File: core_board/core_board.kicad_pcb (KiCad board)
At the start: 2 copper layers, 85.5 x 104 mm, 111 parts, among them J1 Molex_Megafit_02, J10 Conn_01x04_Pin, J11 Conn_01x02_Pin, J12 Conn_01x02_Pin, J13 Conn_01x03_Pin, J14 Conn_01x02_Pin, J15 Conn_01x02_Pin, J16 Conn_01x03_Pin, J2 RJ45_LED_Shielded, J3 Conn_01x02_Pin, J4Serv1 Conn_01x04_Pin, J5 Conn_01x04_Pin, J6 Conn_01x02_Pin, J8 Conn_01x04_Pin, J9 Conn_01x02_Pin, Q1 TPC8132_LQS, Q18 BSS138, Q19 BSS138, Q2 BSS138, Q20 BSS138, Q21 BSS138, Q3 BSS138, Q4 BSS138, Q5 BSS138, Q6 BSS138, Q7 BSS138, SW1 SW_Push, SW2 SW_Push, SW3 SW_Push, SW4 SW_Push, U1 AP63301WU7, U4 BD9G401EFJ-E2

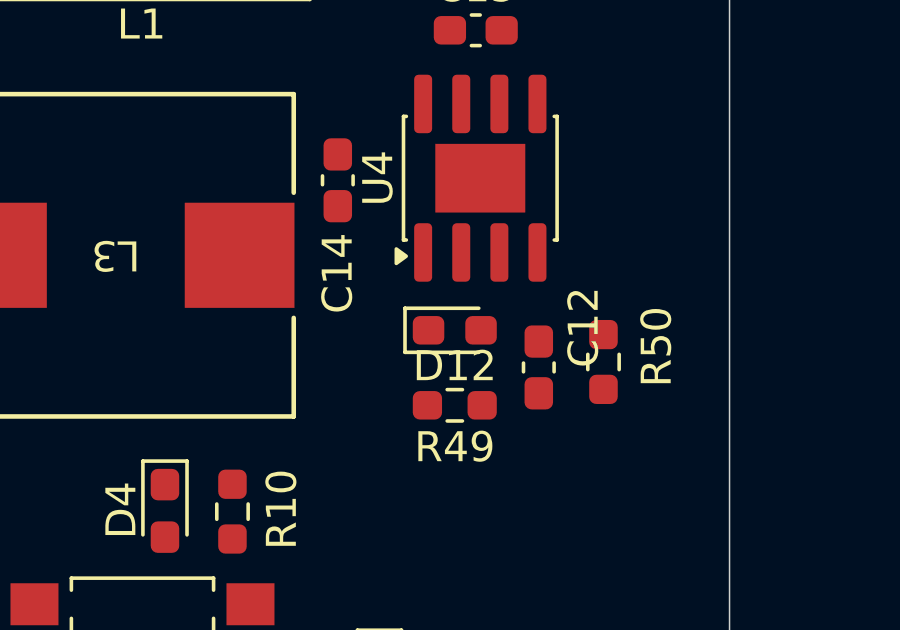
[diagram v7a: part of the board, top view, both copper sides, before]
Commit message: Fix buck circuit values
nothing had values, so I added them
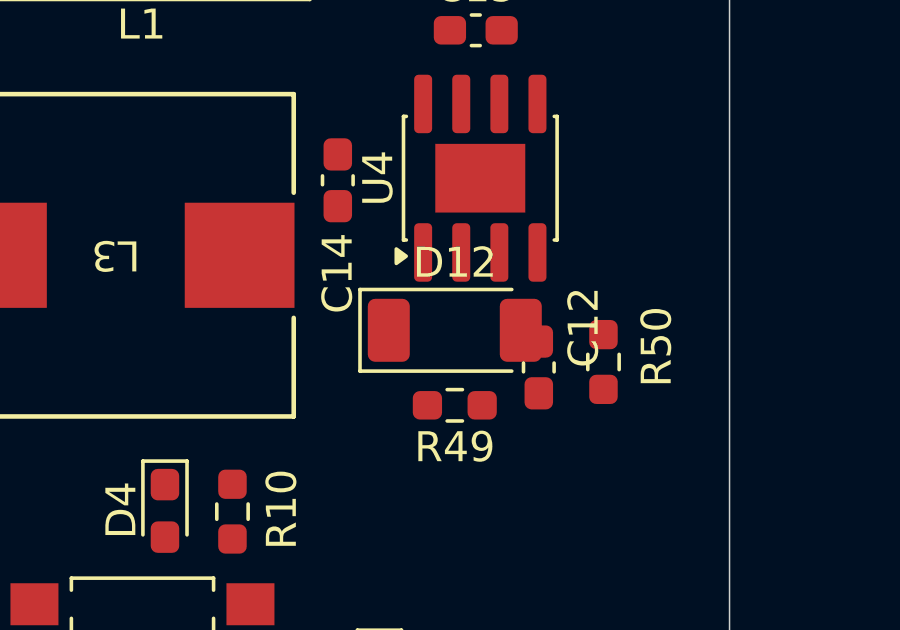
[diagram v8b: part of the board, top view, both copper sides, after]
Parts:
- C12: value C_Small -> 0.01uF
- C13: value C_Small -> 47uF
- C14: value C_Small -> 0.1uF
- C15: value C_Small -> 10uF
- D12: value MMSZ5240BT1G -> PMEG4050EP,115; footprint LED_SMD:LED_0603_1608Metric_Pad1.05x0.95mm_HandSolder -> Diode_SMD:D_SOD-128
- R48: value R_US -> 160k
- R49: value R_US -> 30k
- R50: value R_US -> 4.7k
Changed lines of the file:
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@@
 		)
 	)
-	(footprint "LED_SMD:LED_0603_1608Metric_Pad1.05x0.95mm_HandSolder"
+	(footprint "Diode_SMD:D_SOD-128"
 		(layer "F.Cu")
 		(at 183.8422 58.8626)
-		(descr "LED SMD 0603 (1608 Metric), square (rectangular) end terminal, IPC-7351 nominal, (Body size source: http://www.tortai-tech.com/upload/download/2011102023233369053.pdf)")
-		(tags "LED handsolder")
+		(descr "D_SOD-128 (CFP5 SlimSMAW), https://assets.nexperia.com/documents/outline-drawing/SOD128.pdf")
+		(tags "D_SOD-128")
 		(property "Reference" "D12"
-			(at 0 1.2 0)
+			(at 0 -2.25 0)
 			(layer "F.SilkS")
 			(effects
@@
 			)
 		)
-		(property "Value" "MMSZ5240BT1G"
-			(at -0.0125 1.5 0)
+		(property "Value" "PMEG4050EP,115"
+			(at 0 2.25 0)
 			(layer "F.Fab")
 			(effects
@@
 			)
 		)
-		(property "Datasheet" "https://www.onsemi.com/pdf/datasheet/mmsz5221bt1-d.pdf"
+		(property "Datasheet" "https://assets.nexperia.com/documents/data-sheet/PMEG4050EP.pdf"
 			(at 0 0 0)
+			(unlocked yes)
 			(layer "F.Fab")
 			(hide yes)
@@
 				(font
 					(size 1.27 1.27)
+					(thickness 0.15)
 				)
 			)
@@
 		(property "Description" ""
 			(at 0 0 0)
+			(unlocked yes)
 			(layer "F.Fab")
 			(hide yes)
@@
 				(font
 					(size 1.27 1.27)
-				)
-			)
-		)
-		(property "KiLib_Generator" "SMD_2terminal_chip_molded"
-			(at 0 0 0)
-			(layer "F.SilkS")
-			(hide yes)
-			(effects
-				(font
-					(size 1 1)
 					(thickness 0.15)
 				)
@@
 		(duplicate_pad_numbers_are_jumpers no)
 		(fp_line
-			(start -1.66 -0.735)
-			(end -1.66 0.735)
+			(start -3.16 -1.36)
+			(end -3.16 1.36)
 			(stroke
 				(width 0.12)
@@
 		)
 		(fp_line
-			(start -1.66 0.735)
-			(end 0.8 0.735)
+			(start -3.16 -1.36)
+			(end 1.9 -1.36)
 			(stroke
 				(width 0.12)
@@
 		)
 		(fp_line
-			(start 0.8 -0.735)
-			(end -1.66 -0.735)
+			(start -3.16 1.36)
+			(end 1.9 1.36)
 			(stroke
 				(width 0.12)
@@
 			(layer "F.SilkS")
 		)
-		(fp_rect
-			(start -1.65 -0.73)
-			(end 1.65 0.73)
+		(fp_line
+			(start -3.15 -1.5)
+			(end -3.15 1.5)
 			(stroke
 				(width 0.05)
 				(type solid)
 			)
-			(fill no)
 			(layer "F.CrtYd")
 		)
 		(fp_line
-			(start -0.8 -0.1)
-			(end -0.8 0.4)
+			(start -3.15 -1.5)
+			(end 3.15 -1.5)
+			(stroke
+				(width 0.05)
+				(type solid)
+			)
+			(layer "F.CrtYd")
+		)
+		(fp_line
+			(start 3.15 -1.5)
+			(end 3.15 1.5)
+			(stroke
+				(width 0.05)
+				(type solid)
+			)
+			(layer "F.CrtYd")
+		)
+		(fp_line
+			(start 3.15 1.5)
+			(end -3.15 1.5)
+			(stroke
+				(width 0.05)
+				(type solid)
+			)
+			(layer "F.CrtYd")
+		)
+		(fp_line
+			(start -1.9 -1.25)
+			(end 1.9 -1.25)
 			(stroke
 				(width 0.1)
@@
 		)
 		(fp_line
-			(start -0.8 0.4)
-			(end 0.8 0.4)
+			(start -1.9 1.25)
+			(end -1.9 -1.25)
 			(stroke
 				(width 0.1)
@@
 		)
 		(fp_line
-			(start -0.5 -0.4)
-			(end -0.8 -0.1)
+			(start -0.75 0)
+			(end -0.35 0)
 			(stroke
 				(width 0.1)
@@
 		)
 		(fp_line
-			(start 0.8 -0.4)
-			(end -0.5 -0.4)
+			(start -0.35 0)
+			(end -0.35 -0.55)
 			(stroke
 				(width 0.1)
@@
 		)
 		(fp_line
-			(start 0.8 0.4)
-			(end 0.8 -0.4)
+			(start -0.35 0)
+			(end -0.35 0.55)
+			(stroke
+				(width 0.1)
+				(type solid)
+			)
+			(layer "F.Fab")
+		)
+		(fp_line
+			(start -0.35 0)
+			(end 0.25 -0.4)
+			(stroke
+				(width 0.1)
+				(type solid)
+			)
+			(layer "F.Fab")
+		)
+		(fp_line
+			(start 0.25 -0.4)
+			(end 0.25 0.4)
+			(stroke
+				(width 0.1)
+				(type solid)
+			)
+			(layer "F.Fab")
+		)
+		(fp_line
+			(start 0.25 0)
+			(end 0.75 0)
+			(stroke
+				(width 0.1)
+				(type solid)
+			)
+			(layer "F.Fab")
+		)
+		(fp_line
+			(start 0.25 0.4)
+			(end -0.35 0)
+			(stroke
+				(width 0.1)
+				(type solid)
+			)
+			(layer "F.Fab")
+		)
+		(fp_line
+			(start 1.9 -1.25)
+			(end 1.9 1.25)
+			(stroke
+				(width 0.1)
+				(type solid)
+			)
+			(layer "F.Fab")
+		)
+		(fp_line
+			(start 1.9 1.25)
+			(end -1.9 1.25)
 			(stroke
 				(width 0.1)
@@
 		)
 		(fp_text user "${REFERENCE}"
-			(at 0 0 0)
+			(at 0 -2.25 0)
 			(layer "F.Fab")
 			(effects
 				(font
-					(size 0.4 0.4)
-					(thickness 0.06)
+					(size 1 1)
+					(thickness 0.15)
 				)
 			)
 		)
 		(pad "1" smd roundrect
-			(at -0.875 0)
-			(size 1.05 0.95)
+			(at -2.2 0)
+			(size 1.4 2.1)
 			(layers "F.Cu" "F.Mask" "F.Paste")
-			(roundrect_rratio 0.25)
+			(roundrect_rratio 0.1785714286)
 			(net "Net-(U4-LX)")
 			(pintype "unspecified")
 		)
 		(pad "2" smd roundrect
-			(at 0.875 0)
-			(size 1.05 0.95)
+			(at 2.2 0)
+			(size 1.4 2.1)
 			(layers "F.Cu" "F.Mask" "F.Paste")
-			(roundrect_rratio 0.25)
+			(roundrect_rratio 0.1785714286)
 			(net "GND")
 			(pintype "unspecified")
 		)
 		(embedded_fonts no)
-		(model "${KICAD10_3DMODEL_DIR}/LED_SMD.3dshapes/LED_0603_1608Metric.step"
+		(model "${KICAD9_3DMODEL_DIR}/Diode_SMD.3dshapes/D_SOD-128.step"
 			(offset
 				(xyz 0 0 0)
@@
 			)
 		)
-		(property "Value" "C_Small"
+		(property "Value" "47uF"
 			(at 0 1.43 90)
 			(layer "F.Fab")
@@
 			)
 		)
-		(property "Value" "R_US"
+		(property "Value" "4.7k"
 			(at 0 1.43 90)
 			(layer "F.Fab")
@@
 			)
 		)
-		(property "Value" "R_US"
+		(property "Value" "30k"
 			(at 0.0125 2.7 0)
 			(layer "F.Fab")
@@
 			)
 		)
-		(property "Value" "C_Small"
+		(property "Value" "0.1uF"
 			(at 0 1.43 90)
 			(layer "F.Fab")
@@
 			)
 		)
-		(property "Value" "R_US"
+		(property "Value" "160k"
 			(at 0 1.43 0)
 			(layer "F.Fab")
@@
 			)
 		)
-		(property "Value" "C_Small"
+		(property "Value" "0.01uF"
 			(at 0 1.43 90)
 			(layer "F.Fab")
@@
 			)
 		)
-		(property "Value" "C_Small"
+		(property "Value" "10uF"
 			(at 0 1.43 0)
 			(layer "F.Fab")
